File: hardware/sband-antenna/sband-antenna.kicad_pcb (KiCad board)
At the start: 2 copper layers, 98 x 98 mm, 7 parts, among them J1 CONMCX002-SMD

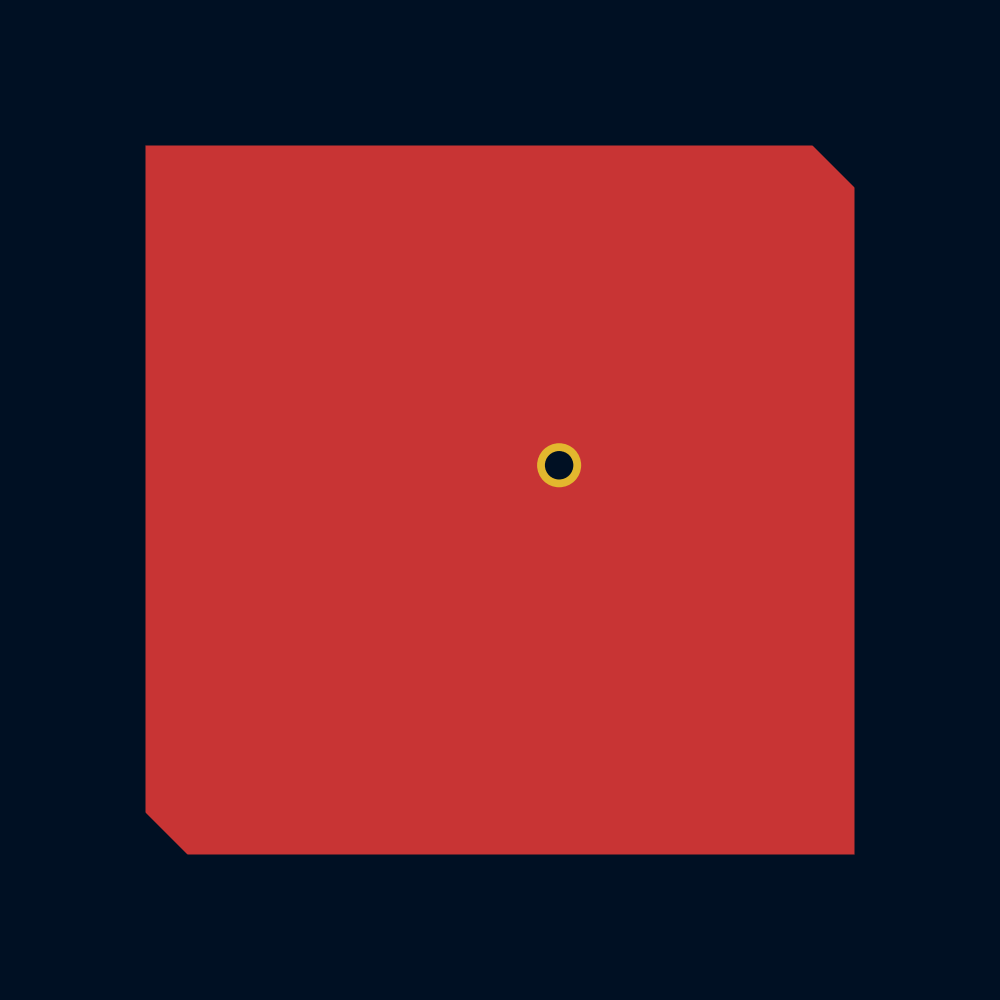
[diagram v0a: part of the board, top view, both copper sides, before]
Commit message: main: hardware: Frequency band adjustments
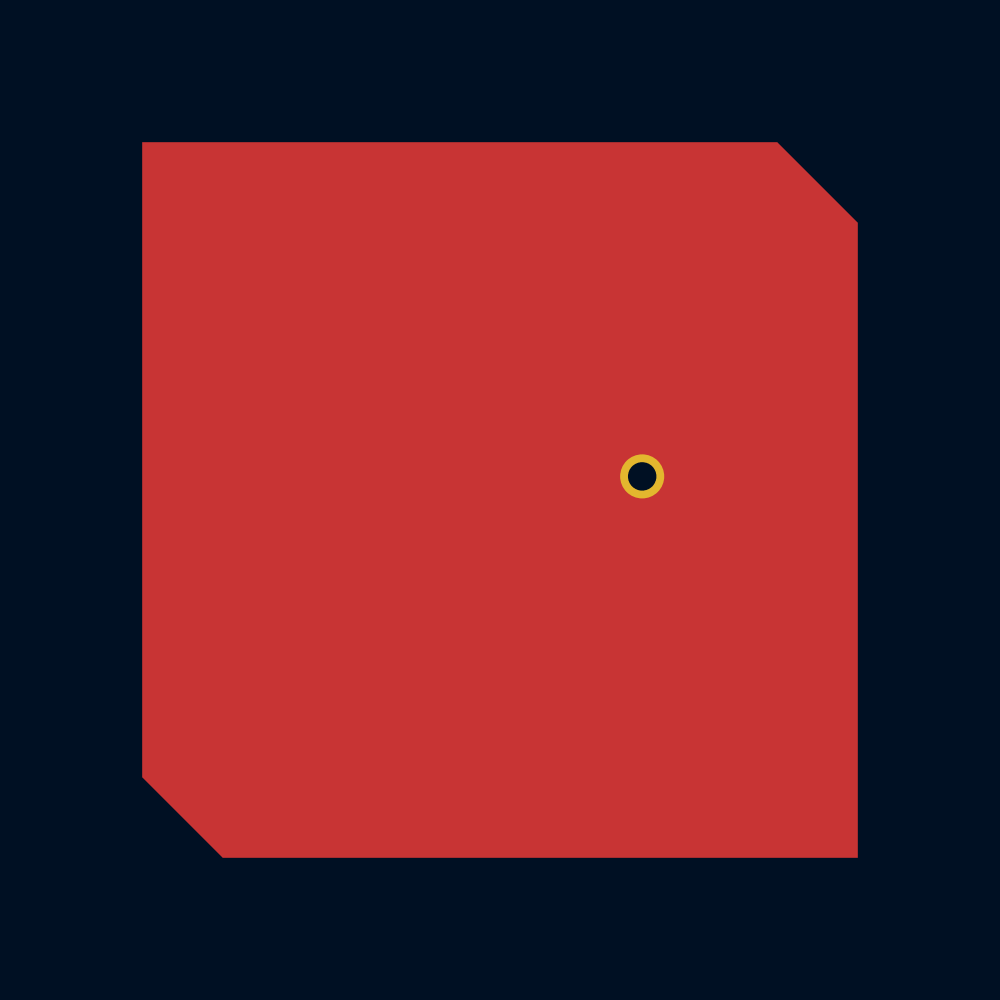
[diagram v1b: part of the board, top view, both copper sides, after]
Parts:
- moved J1 3.54 mm to (109.4, 94.5)
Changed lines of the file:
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@@
 			(psa4output no)
 			(plot_black_and_white yes)
-			(plotinvisibletext no)
 			(sketchpadsonfab no)
 			(plotpadnumbers no)
@@
 		(pad "1" smd roundrect
 			(at 0 0)
-			(size 29.92 29.92)
+			(size 30.2 30.2)
 			(layers "F.Cu" "F.Mask")
 			(roundrect_rratio 0)
-			(chamfer_ratio 0.0592)
+			(chamfer_ratio 0.1125827815)
 			(chamfer top_right bottom_left)
 			(net 2 "ant")
@@
 	(footprint "spacelab_lib:LINX_CONMCX002-SMD"
 		(layer "B.Cu")
-		(at 105.864773 94.032334 90)
+		(at 109.369773 94.502334 90)
 		(property "Reference" "J1"
 			(at 0 -4.73 270)
@@
 		(layer "Edge.Cuts")
 	)
+	(dimension
+		(type orthogonal)
+		(layer "User.1")
+		(pts
+			(xy 105.864773 94.502334) (xy 105.874773 110.602334)
+		)
+		(height 0)
+		(orientation 1)
+		(format
+			(prefix "")
+			(suffix "")
+			(units 3)
+			(units_format 1)
+			(precision 4)
+		)
+		(style
+			(thickness 0.15)
+			(arrow_length 1.27)
+			(text_position_mode 0)
+			(arrow_direction outward)
+			(extension_height 0.58642)
+			(extension_offset 0.5)
+			(keep_text_aligned yes)
+		)
+		(gr_text "16.1000 mm"
+			(at 104.714773 102.552334 90)
+			(layer "User.1")
+			(effects
+				(font
+					(size 1 1)
+					(thickness 0.15)
+				)
+			)
+		)
+	)
+	(dimension
+		(type orthogonal)
+		(layer "User.1")
+		(pts
+			(xy 105.864773 94.502334) (xy 105.864773 80.402334)
+		)
+		(height 0)
+		(orientation 1)
+		(format
+			(prefix "")
+			(suffix "")
+			(units 3)
+			(units_format 1)
+			(precision 4)
+		)
+		(style
+			(thickness 0.15)
+			(arrow_length 1.27)
+			(text_position_mode 0)
+			(arrow_direction outward)
+			(extension_height 0.58642)
+			(extension_offset 0.5)
+			(keep_text_aligned yes)
+		)
+		(gr_text "14.1000 mm"
+			(at 104.714773 87.452334 90)
+			(layer "User.1")
+			(effects
+				(font
+					(size 1 1)
+					(thickness 0.15)
+				)
+			)
+		)
+	)
+	(dimension
+		(type orthogonal)
+		(layer "User.1")
+		(pts
+			(xy 115.369773 94.502334) (xy 88.264773 94.862334)
+		)
+		(height -0.01)
+		(orientation 0)
+		(format
+			(prefix "")
+			(suffix "")
+			(units 3)
+			(units_format 1)
+			(precision 4)
+		)
+		(style
+			(thickness 0.15)
+			(arrow_length 1.27)
+			(text_position_mode 0)
+			(arrow_direction outward)
+			(extension_height 0.58642)
+			(extension_offset 0.5)
+			(keep_text_aligned yes)
+		)
+		(gr_text "27.1050 mm"
+			(at 101.817273 93.342334 0)
+			(layer "User.1")
+			(effects
+				(font
+					(size 1 1)
+					(thickness 0.15)
+				)
+			)
+		)
+	)
+	(dimension
+		(type orthogonal)
+		(layer "User.1")
+		(pts
+			(xy 115.369773 94.502334) (xy 118.474773 93.982334)
+		)
+		(height 0)
+		(orientation 0)
+		(format
+			(prefix "")
+			(suffix "")
+			(units 3)
+			(units_format 1)
+			(precision 4)
+		)
+		(style
+			(thickness 0.15)
+			(arrow_length 1.27)
+			(text_position_mode 0)
+			(arrow_direction outward)
+			(extension_height 0.58642)
+			(extension_offset 0.5)
+			(keep_text_aligned yes)
+		)
+		(gr_text "3.1050 mm"
+			(at 116.922273 93.352334 0)
+			(layer "User.1")
+			(effects
+				(font
+					(size 1 1)
+					(thickness 0.15)
+				)
+			)
+		)
+	)
 	(via
 		(at 61.184375 133.430759)
@@
 		(polygon
 			(pts
-				(xy 107.419996 93.909935) (xy 107.381701 93.668152) (xy 107.306055 93.435336) (xy 107.194919 93.21722)
-				(xy 107.051031 93.019174) (xy 106.877933 92.846076) (xy 106.679887 92.702188) (xy 106.461771 92.591052)
-				(xy 106.228955 92.515406) (xy 105.987172 92.477111) (xy 105.742374 92.477111) (xy 105.500591 92.515406)
-				(xy 105.267775 92.591052) (xy 105.049659 92.702188) (xy 104.851613 92.846076) (xy 104.678515 93.019174)
-				(xy 104.534627 93.21722) (xy 104.423491 93.435336) (xy 104.347845 93.668152) (xy 104.30955 93.909935)
-				(xy 104.30955 94.154733) (xy 104.347845 94.396516) (xy 104.423491 94.629332) (xy 104.534627 94.847448)
-				(xy 104.678515 95.045494) (xy 104.851613 95.218592) (xy 105.049659 95.36248) (xy 105.267775 95.473616)
-				(xy 105.500591 95.549262) (xy 105.742374 95.587557) (xy 105.987172 95.587557) (xy 106.228955 95.549262)
-				(xy 106.461771 95.473616) (xy 106.679887 95.36248) (xy 106.877933 95.218592) (xy 107.051031 95.045494)
-				(xy 107.194919 94.847448) (xy 107.306055 94.629332) (xy 107.381701 94.396516) (xy 107.419996 94.154733)
-			)
-		)
+				(xy 110.926994 94.384712) (xy 110.888699 94.142929) (xy 110.813053 93.910113) (xy 110.701917 93.691997)
+				(xy 110.558029 93.493951) (xy 110.384931 93.320853) (xy 110.186885 93.176965) (xy 109.968769 93.065829)
+				(xy 109.735953 92.990183) (xy 109.49417 92.951888) (xy 109.249372 92.951888) (xy 109.007589 92.990183)
+				(xy 108.774773 93.065829) (xy 108.556657 93.176965) (xy 108.358611 93.320853) (xy 108.185513 93.493951)
+				(xy 108.041625 93.691997) (xy 107.930489 93.910113) (xy 107.854843 94.142929) (xy 107.816548 94.384712)
+				(xy 107.816548 94.62951) (xy 107.854843 94.871293) (xy 107.930489 95.104109) (xy 108.041625 95.322225)
+				(xy 108.185513 95.520271) (xy 108.358611 95.693369) (xy 108.556657 95.837257) (xy 108.774773 95.948393)
+				(xy 109.007589 96.024039) (xy 109.249372 96.062334) (xy 109.49417 96.062334) (xy 109.735953 96.024039)
+				(xy 109.968769 95.948393) (xy 110.186885 95.837257) (xy 110.384931 95.693369) (xy 110.558029 95.520271)
+				(xy 110.701917 95.322225) (xy 110.813053 95.104109) (xy 110.888699 94.871293) (xy 110.926994 94.62951)
+			)
+		)
